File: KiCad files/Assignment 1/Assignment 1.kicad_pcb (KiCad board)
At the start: 2 copper layers, 5 parts, among them SW1 SW_Push, SW2 SW_Push, U1 CC56-12EWA

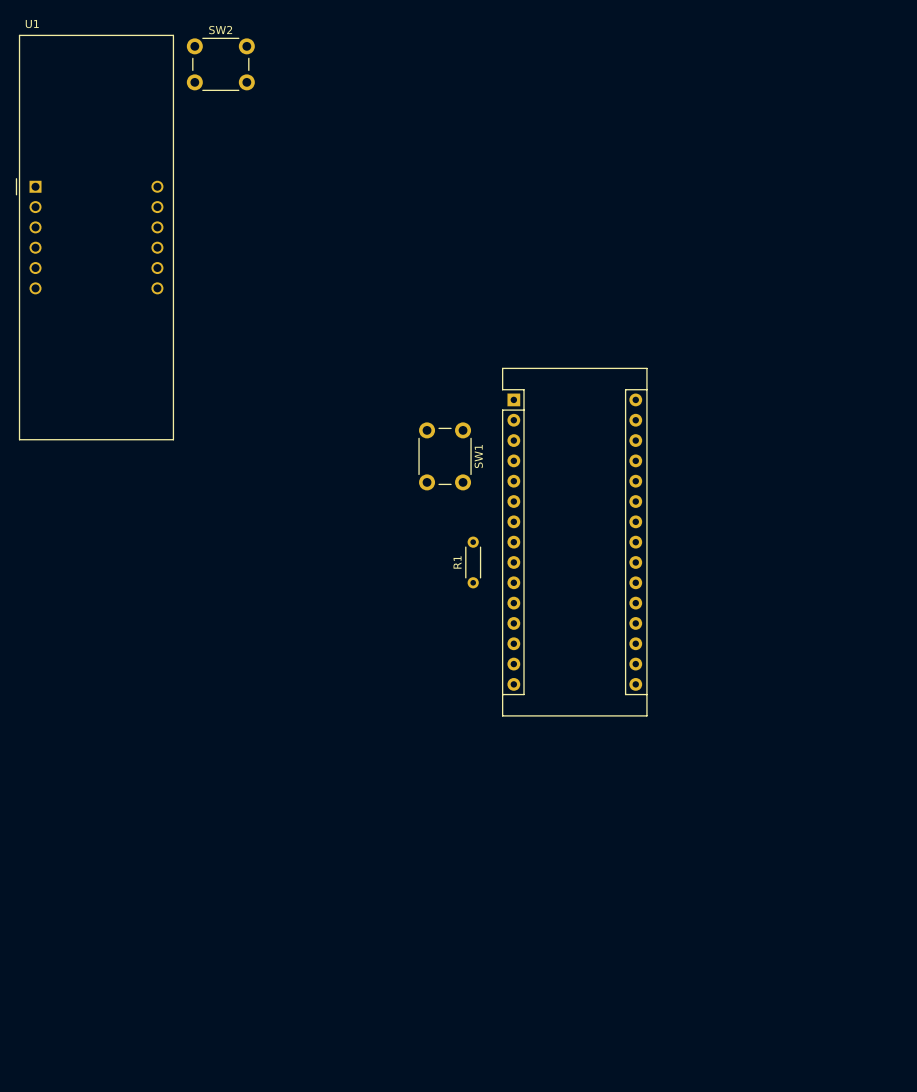
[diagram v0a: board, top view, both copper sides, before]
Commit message: Fixed KiCad project file clash issue Added code to ReadMe
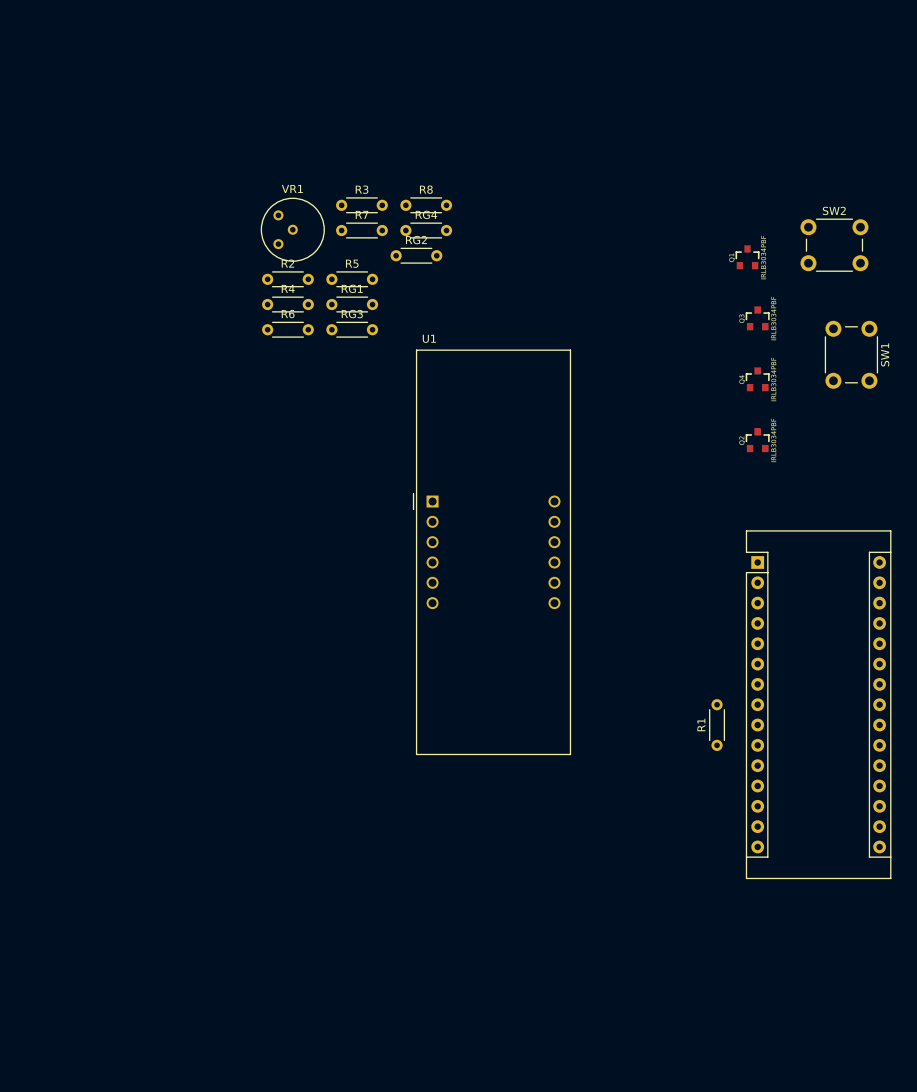
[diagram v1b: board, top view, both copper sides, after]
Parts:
- added Q1: IRLB3034PBF, Silicon-Standard:SOT23-3, F.Cu at (91.4, 27.9)
- added Q2: IRLB3034PBF, Silicon-Standard:SOT23-3, F.Cu at (92.7, 50.8)
- added Q3: IRLB3034PBF, Silicon-Standard:SOT23-3, F.Cu at (92.7, 35.6)
- added Q4: IRLB3034PBF, Silicon-Standard:SOT23-3, F.Cu at (92.7, 43.2)
- added R2: 330 Ω, Resistor_THT:R_Axial_DIN0204_L3.6mm_D1.6mm_P5.08mm_Horizontal, F.Cu at (31.5, 30.6)
- added R3: 330 Ω, Resistor_THT:R_Axial_DIN0204_L3.6mm_D1.6mm_P5.08mm_Horizontal, F.Cu at (40.7, 21.4)
- added R4: 330 Ω, Resistor_THT:R_Axial_DIN0204_L3.6mm_D1.6mm_P5.08mm_Horizontal, F.Cu at (31.5, 33.8)
- added R5: 330 Ω, Resistor_THT:R_Axial_DIN0204_L3.6mm_D1.6mm_P5.08mm_Horizontal, F.Cu at (39.5, 30.6)
- added R6: 330 Ω, Resistor_THT:R_Axial_DIN0204_L3.6mm_D1.6mm_P5.08mm_Horizontal, F.Cu at (31.5, 36.9)
- added R7: 330 Ω, Resistor_THT:R_Axial_DIN0204_L3.6mm_D1.6mm_P5.08mm_Horizontal, F.Cu at (40.7, 24.5)
- added R8: 330 Ω, Resistor_THT:R_Axial_DIN0204_L3.6mm_D1.6mm_P5.08mm_Horizontal, F.Cu at (48.7, 21.4)
- added RG1: 5.6k, Resistor_THT:R_Axial_DIN0204_L3.6mm_D1.6mm_P5.08mm_Horizontal, F.Cu at (39.5, 33.8)
- added RG2: 5.6k, Resistor_THT:R_Axial_DIN0204_L3.6mm_D1.6mm_P5.08mm_Horizontal, F.Cu at (47.5, 27.7)
- added RG3: 5.6k, Resistor_THT:R_Axial_DIN0204_L3.6mm_D1.6mm_P5.08mm_Horizontal, F.Cu at (39.5, 36.9)
- added RG4: 5.6k, Resistor_THT:R_Axial_DIN0204_L3.6mm_D1.6mm_P5.08mm_Horizontal, F.Cu at (48.7, 24.5)
- added VR1: POTENTIOMETER-PTH-9MM-1_20W-20%, Potentiometer_THT:Potentiometer_Bourns_3339H_Vertical, F.Cu at (32.8, 26.2)
- R1: value 1k -> 330 Ω
- moved SW2 80.0 mm to (99.1, 24.1)
- moved U1 63.3 mm to (52.1, 58.4)
- moved SW1 52.4 mm to (106.7, 36.8)
- moved A1 36.6 mm to (92.7, 66.0)
- moved R1 36.6 mm to (87.6, 88.9)
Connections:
- net Net-(A1-Pad27) renamed 5V
- net Net-(A1-Pad29) renamed GND
- A1 pad 10: Net-(A1-Pad10) -> Segment_F_anode
- A1 pad 11: Net-(A1-Pad11) -> Segment_G_anode
- A1 pad 12: Net-(A1-Pad12) -> Segment_DP_anode
- A1 pad 13: Net-(A1-Pad13) -> Digit_1_cathode
- A1 pad 14: Net-(A1-Pad14) -> Digit_3_cathode
- A1 pad 15: Net-(A1-Pad15) -> Digit_2_cathode
- A1 pad 19: Net-(A1-Pad19) -> Digit_4_cathode
- A1 pad 20: Net-(A1-Pad20) -> Segment_A_anode
- A1 pad 21: Net-(A1-Pad21) -> Segment_B_anode
- A1 pad 7: Net-(A1-Pad7) -> Segment_C_anode
- A1 pad 8: Net-(A1-Pad8) -> Segment_D_anode
- A1 pad 9: Net-(A1-Pad9) -> Segment_E_anode
- R1 pad 1: Net-(R1-Pad1) -> Segment_A_anode
- SW1 pad 2: Net-(A1-Pad6) -> Net-(A1-Pad5)
- SW2 pad 2: Net-(A1-Pad5) -> Net-(A1-Pad6)
- U1 pad 11: Net-(U1-Pad11) -> Net-(R1-Pad2)

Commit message: Added images of the schematic and the 3D view
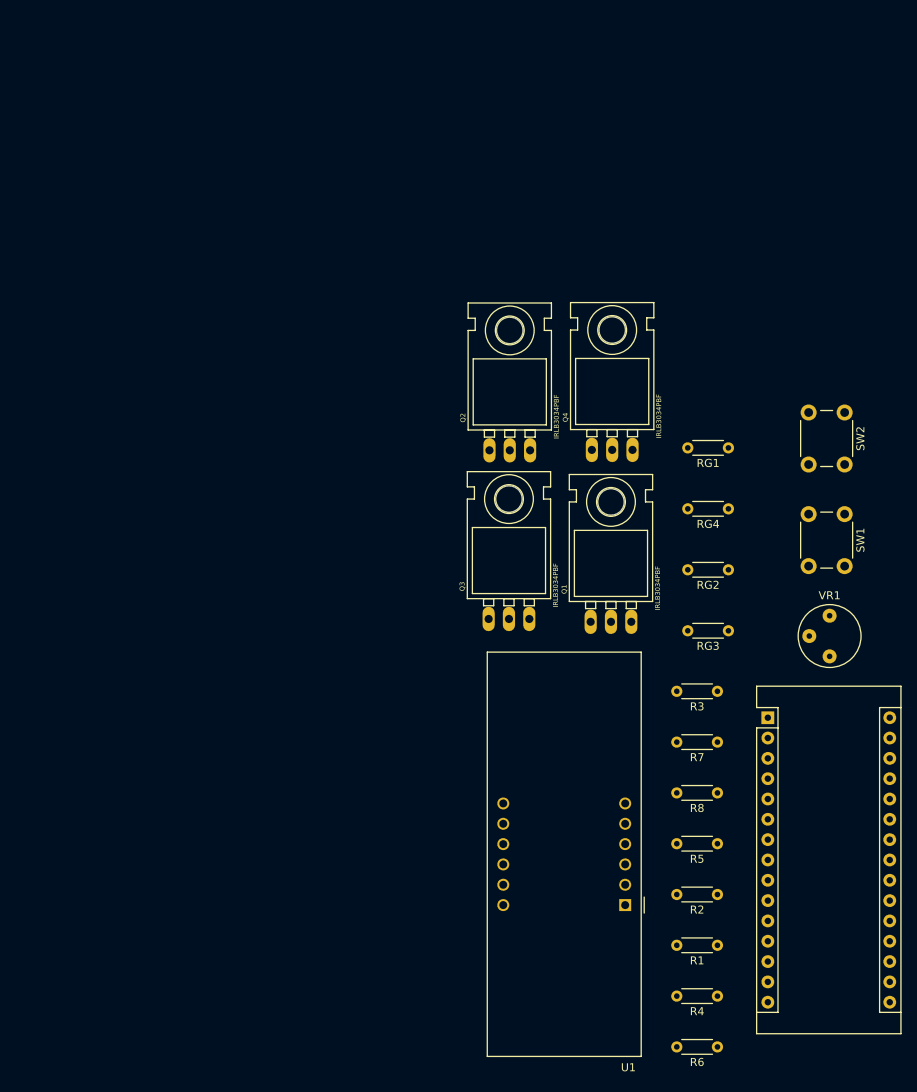
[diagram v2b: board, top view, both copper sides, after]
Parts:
- Q1, Q2, Q3, Q4: footprint Silicon-Standard:SOT23-3 -> Silicon-Standard:TO-220-ALT
- VR1: footprint Potentiometer_THT:Potentiometer_Bourns_3339H_Vertical -> Potentiometer_THT:Potentiometer_Bourns_3339P_Vertical_HandSoldering
- moved R6 105.8 mm to (87.7, 126.6), turned to 180 degrees
- moved R4 103.1 mm to (87.7, 120.2), turned to 180 degrees
- moved R2 95.3 mm to (87.7, 107.5), turned to 180 degrees
- moved VR1 86.0 mm to (101.7, 77.8)
- moved R5 85.4 mm to (87.7, 101.2), turned to 180 degrees
- moved R8 83.1 mm to (87.7, 94.8), turned to 180 degrees
- moved R7 79.3 mm to (87.7, 88.5), turned to 180 degrees
- moved R3 76.8 mm to (87.7, 82.1), turned to 180 degrees
- moved RG3 62.2 mm to (89.1, 74.6), turned to 180 degrees
- moved RG2 57.2 mm to (89.1, 67.0), turned to 180 degrees
- moved U1 55.9 mm to (76.1, 108.9), turned to 180 degrees
- moved RG4 53.3 mm to (89.1, 59.3), turned to 180 degrees
- moved RG1 52.7 mm to (89.1, 51.7), turned to 180 degrees
- moved Q3 45.9 mm to (61.6, 69.3)
- moved Q1 45.1 mm to (74.4, 69.6)
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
